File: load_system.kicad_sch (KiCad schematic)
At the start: 1 part

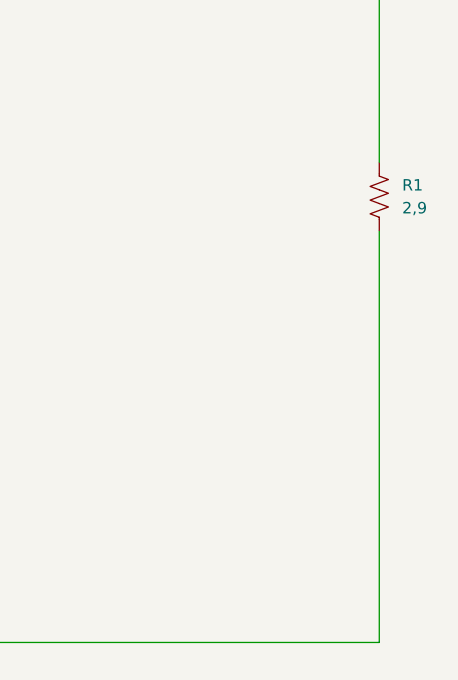
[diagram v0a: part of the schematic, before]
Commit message: feat: new Circuit elements in the schematic and new LTspice Model
feat:added latch in kicad schematic with relative sheet

feat:added Analog-comparator in kicad schematic

feat:added LTspice Analog-comparator model

feat:added spice model into Models folder for the Analog_comparator

refactor:moved all LTspice simulation in a single folder for each one
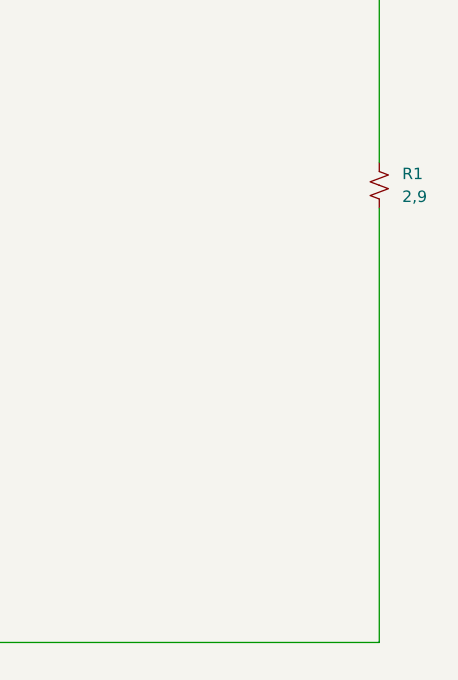
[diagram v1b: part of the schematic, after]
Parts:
- removed R1: 2,9, symbol Device:R_US
- added R1: 2,9, symbol Device:R_Small_US
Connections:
- net LOAD_SUPPLY_IN: now also R1.1
- net LOAD_SUPPLY_OUT: now also R1.2
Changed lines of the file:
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@@
 	(wire
 		(pts
-			(xy 109.22 101.6) (xy 109.22 147.32)
+			(xy 109.22 99.06) (xy 109.22 147.32)
 		)
 		(stroke
@@
 	)
 	(symbol
-		(lib_id "Device:R_US")
-		(at 109.22 97.79 0)
+		(lib_id "Device:R_Small_US")
+		(at 109.22 96.52 0)
 		(unit 1)
 		(exclude_from_sim no)
@@
 		(fields_autoplaced yes)
 		(property "Reference" "R1"
-			(at 111.76 96.5199 0)
+			(at 111.76 95.2499 0)
 			(effects
 				(font
@@
 		)
 		(property "Value" "2,9"
-			(at 111.76 99.0599 0)
+			(at 111.76 97.7899 0)
 			(effects
 				(font
@@
 		)
 		(property "Footprint" ""
-			(at 110.236 98.044 90)
+			(at 109.22 96.52 0)
 			(effects
 				(font
@@
 		)
 		(property "Datasheet" "~"
-			(at 109.22 97.79 0)
+			(at 109.22 96.52 0)
 			(effects
 				(font
@@
 			)
 		)
-		(property "Description" "Resistor, US symbol"
-			(at 109.22 97.79 0)
+		(property "Description" "Resistor, small US symbol"
+			(at 109.22 96.52 0)
 			(effects
 				(font

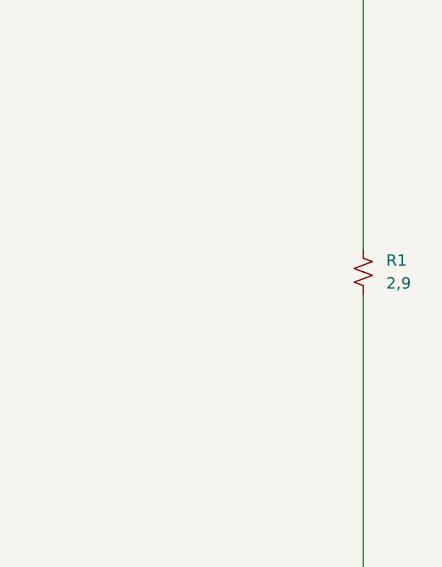
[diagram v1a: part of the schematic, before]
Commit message: feat + fix + refactor on the kicad schematic and simulation folder
feat:added transistor for coil supply

refractor: deleted latch sheet

feat: added latch connection

refractor: the monito logic and the supply are now separated

feat:added labels for connection

feat:added falstad NAND latch simulation

ERC = not tested
DRC = not tested
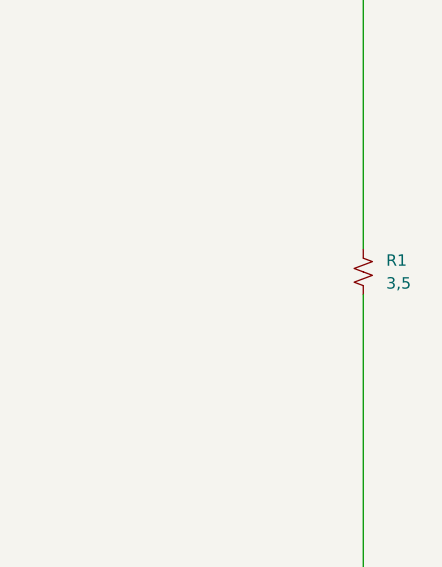
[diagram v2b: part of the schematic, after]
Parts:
- R1: value 2,9 -> 3,5
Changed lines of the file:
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@@
 			)
 		)
-		(property "Value" "2,9"
+		(property "Value" "3,5"
 			(at 111.76 97.7899 0)
 			(effects

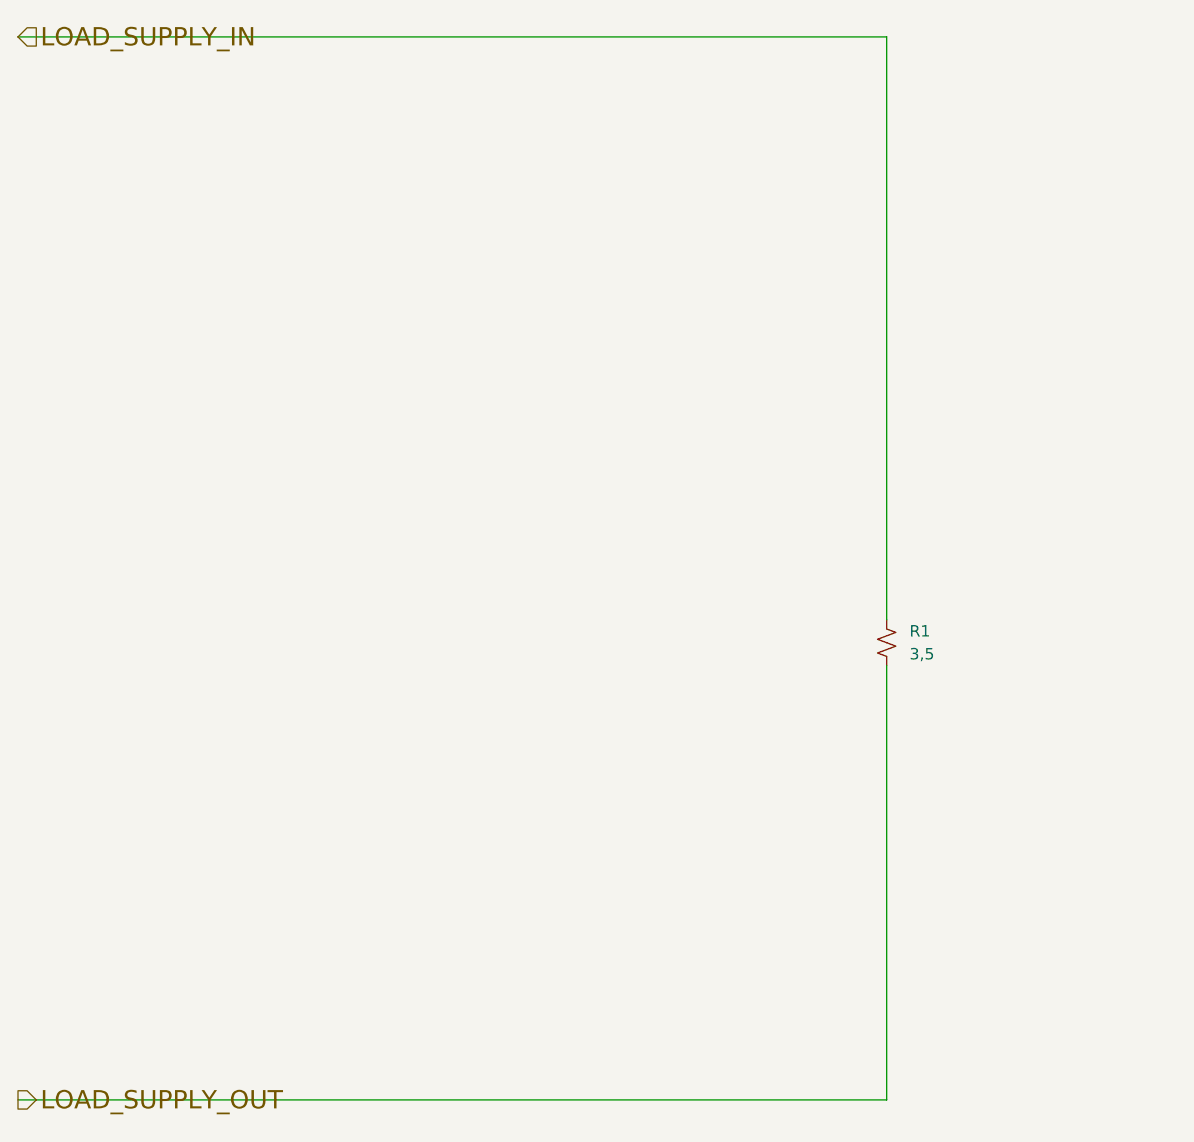
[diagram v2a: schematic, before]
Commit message: feat on the kicad schematic and the simulation folder
feat:added voltage Divider

feat:added ED555 ltSpice simulation

feat:added ED555 power cycle timer connection in kicad schematic

ERC:errors(1) warnings(3)
DRC:not tested
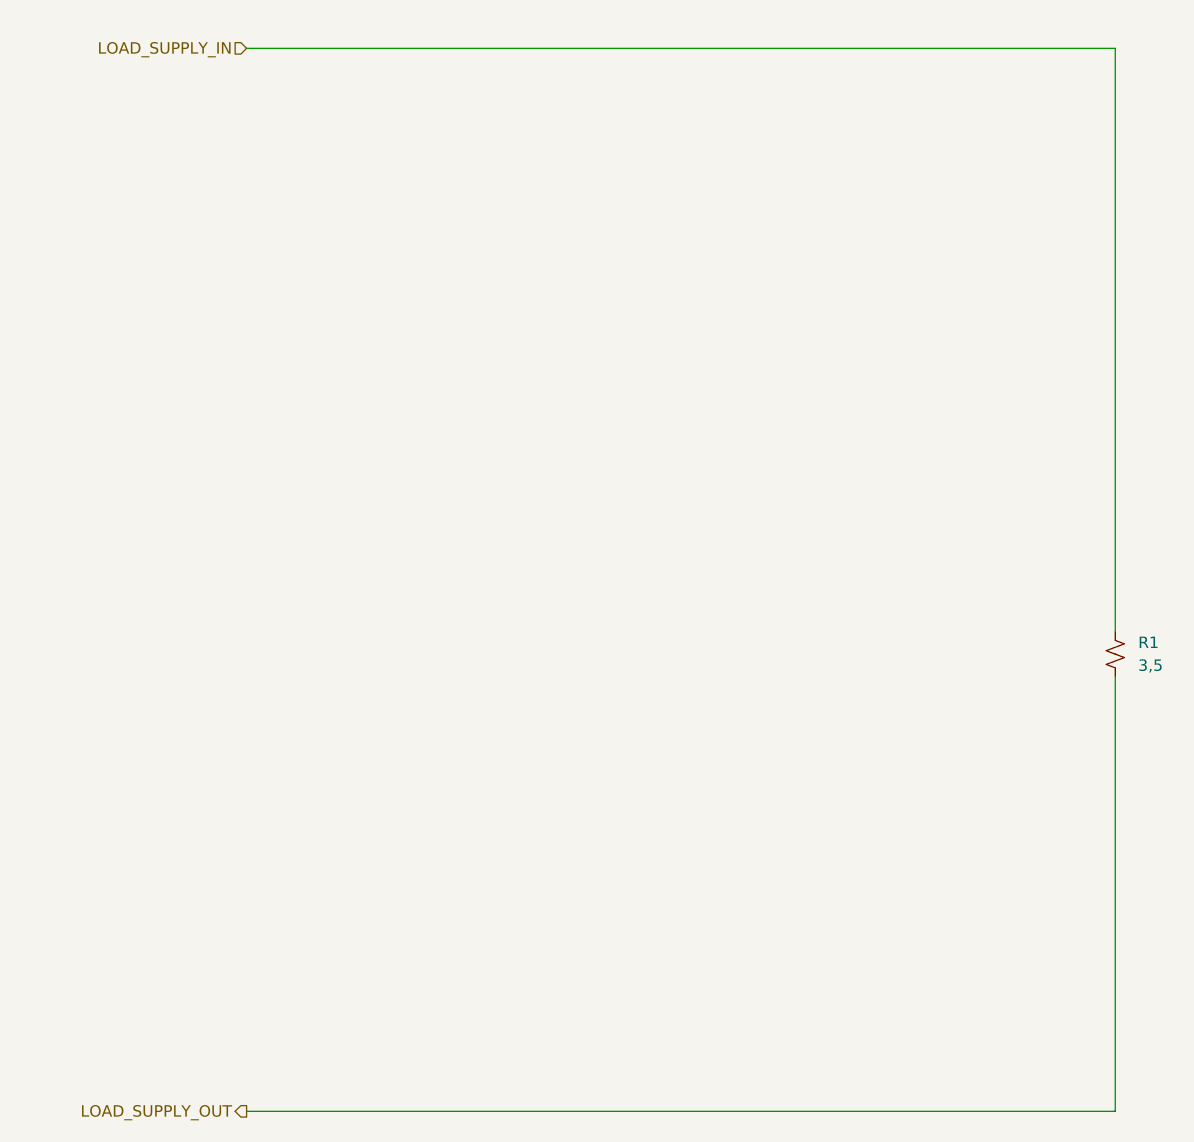
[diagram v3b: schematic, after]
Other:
- moved on the sheet: R1
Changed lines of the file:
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@@
 	(wire
 		(pts
-			(xy 12.7 29.21) (xy 109.22 29.21)
+			(xy 38.1 30.48) (xy 134.62 30.48)
 		)
 		(stroke
@@
 	(wire
 		(pts
-			(xy 109.22 147.32) (xy 12.7 147.32)
+			(xy 134.62 148.59) (xy 38.1 148.59)
 		)
 		(stroke
@@
 	(wire
 		(pts
-			(xy 109.22 29.21) (xy 109.22 93.98)
+			(xy 134.62 30.48) (xy 134.62 95.25)
 		)
 		(stroke
@@
 	(wire
 		(pts
-			(xy 109.22 99.06) (xy 109.22 147.32)
+			(xy 134.62 100.33) (xy 134.62 148.59)
 		)
 		(stroke
@@
 	(hierarchical_label "LOAD_SUPPLY_OUT"
 		(shape output)
-		(at 12.7 147.32 0)
+		(at 38.1 148.59 180)
 		(effects
 			(font
-				(size 2.032 2.032)
+				(size 1.27 1.27)
 			)
-			(justify left)
+			(justify right)
 		)
 	)
 	(hierarchical_label "LOAD_SUPPLY_IN"
 		(shape input)
-		(at 12.7 29.21 0)
+		(at 38.1 30.48 180)
 		(effects
 			(font
-				(size 2.032 2.032)
+				(size 1.27 1.27)
 			)
-			(justify left)
+			(justify right)
 		)
 	)
 	(symbol
 		(lib_id "Device:R_Small_US")
-		(at 109.22 96.52 0)
+		(at 134.62 97.79 0)
 		(unit 1)
 		(exclude_from_sim no)
@@
 		(fields_autoplaced yes)
 		(property "Reference" "R1"
-			(at 111.76 95.2499 0)
+			(at 137.16 96.5199 0)
 			(effects
 				(font
@@
 		)
 		(property "Value" "3,5"
-			(at 111.76 97.7899 0)
+			(at 137.16 99.0599 0)
 			(effects
 				(font
@@
 		)
 		(property "Footprint" ""
-			(at 109.22 96.52 0)
+			(at 134.62 97.79 0)
 			(effects
 				(font
@@
 		)
 		(property "Datasheet" "~"
-			(at 109.22 96.52 0)
+			(at 134.62 97.79 0)
 			(effects
 				(font
@@
 		)
 		(property "Description" "Resistor, small US symbol"
-			(at 109.22 96.52 0)
+			(at 134.62 97.79 0)
 			(effects
 				(font

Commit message: feat + fix on kicad pcb
feat:added mass layer

refactor: moved components for better connection

fix:added missing footprints to resistors etc.

ERC: passed warnings(3)
DRC: errors(42) ;(
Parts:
- R1: footprint (none) -> Resistor_SMD:R_0201_0603Metric
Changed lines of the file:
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@@
 			)
 		)
-		(property "Footprint" ""
+		(property "Footprint" "Resistor_SMD:R_0201_0603Metric"
 			(at 134.62 97.79 0)
 			(effects
